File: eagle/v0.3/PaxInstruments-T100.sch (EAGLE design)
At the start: 32 parts, among them U1 Attiny85

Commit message: Added a bunch of BoM data.
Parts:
- removed L1: (no value), SeeesStudio-OPL:L-0603
- removed LOGO1: SPARKFUN-AESTHETICS_OSHW-LOGOS, PaxInstrument-T400:SPARKFUN-AESTHETICS_OSHW-LOGOS
- added R12: 0R, rcl:R-EU_R0603
- C1, C4, C5, C6, C7: MF (none) -> Yageo; MPN (none) -> CC0603JRX7R9BB104; OC_DIGIKEY (none) -> 311-1779-2-ND; POPULATE (none) -> generic; TOLERANCE (none) -> 5%
- C2, C3: POPULATE (none) -> generic
- C8: MF (none) -> Murata Electronics North America; MPN (none) -> GRM155R60J105KE19D; OC_DIGIKEY (none) -> 490-1320-2-ND; POPULATE (none) -> generic; TOLERANCE (none) -> 10%
- D1, D2: MF (none) -> Diodes Incorporated; MPN (none) -> BZT52C3V6S-7-F; OC_DIGIKEY (none) -> BZT52C3V6S-FDITR-ND; POPULATE (none) -> generic
- JP1: MF (none) -> Molex; MPN (none) -> 0480370001; OC_DIGIKEY (none) -> WM17117-ND; POPULATE (none) -> generic
- JP2: MF (none) -> FCI; MPN (none) -> 95278-101A06LF; OC_DIGIKEY (none) -> 609-3487-2-ND; POPULATE (none) -> DNP
- JP3, U$1: POPULATE (none) -> DNP
- LED1: value (none) -> Green; MF (none) -> Lite-On Inc.; MPN (none) -> LTST-C191KGKT; OC_DIGIKEY (none) -> 160-1446-2-ND; POPULATE (none) -> generic
- R1, R2: MF (none) -> Yageo; MPN (none) -> RC0603JR-0727RL; OC_DIGIKEY (none) -> 311-27GRTR-ND; POPULATE (none) -> generic; TOLERANCE (none) -> 5%
- R10: OC_DIGIKEY (none) -> 311-499DTR-ND; TOLERANCE (none) -> 0.5%
- R11: MF (none) -> Yageo; MPN (none) -> RC0603JR-070RL; OC_DIGIKEY (none) -> 311-0.0GRTR-ND; POPULATE (none) -> generic; TOLERANCE (none) -> Jumper
- R3, R4: MF (none) -> Yageo; MPN (none) -> RC0603FR-071ML; OC_DIGIKEY (none) -> 311-1.00MHRTR-ND; POPULATE (none) -> generic; TOLERANCE (none) -> 1%
- R5, R6: OC_DIGIKEY (none) -> 311-499DTR-ND; POPULATE (none) -> generic; TOLERANCE (none) -> 0.5%
- R7, R8: MF (none) -> Yageo; MPN (none) -> RC0603JR-074K7L; OC_DIGIKEY (none) -> 311-4.7KGRTR-ND; POPULATE (none) -> generic; TOLERANCE (none) -> 5%
- R9: MF (none) -> Yageo; MPN (none) -> RC0603JR-071K2L; OC_DIGIKEY (none) -> 311-1.2KGRTR-ND; POPULATE (none) -> generic; TOLERANCE (none) -> 5%
- U$3: value MCP3421 -> MCP3421A0; MF (none) -> Microchip Technology; MPN (none) -> MCP3421A0T-E/CH; OC_DIGIKEY (none) -> MCP3421A0T-E/CHTR-ND; POPULATE (none) -> MPN
- U$4: MF (none) -> Microchip Technology; MPN (none) -> MCP9800A0T-M/OT; OC_DIGIKEY (none) -> MCP9800A0T-M/OTTR-ND; POPULATE (none) -> MPN
- U$5: MF (none) -> Pax Instruments; POPULATE (none) -> MPN
- U1: MF (none) -> Atmel; MPN (none) -> ATTINY85-20SUR; OC_DIGIKEY (none) -> ATTINY85-20SURTR-ND; POPULATE (none) -> MPN
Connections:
- net A_5V: now also R12.1; no longer L1.2
- net USB_5V: now also R12.2; no longer L1.1

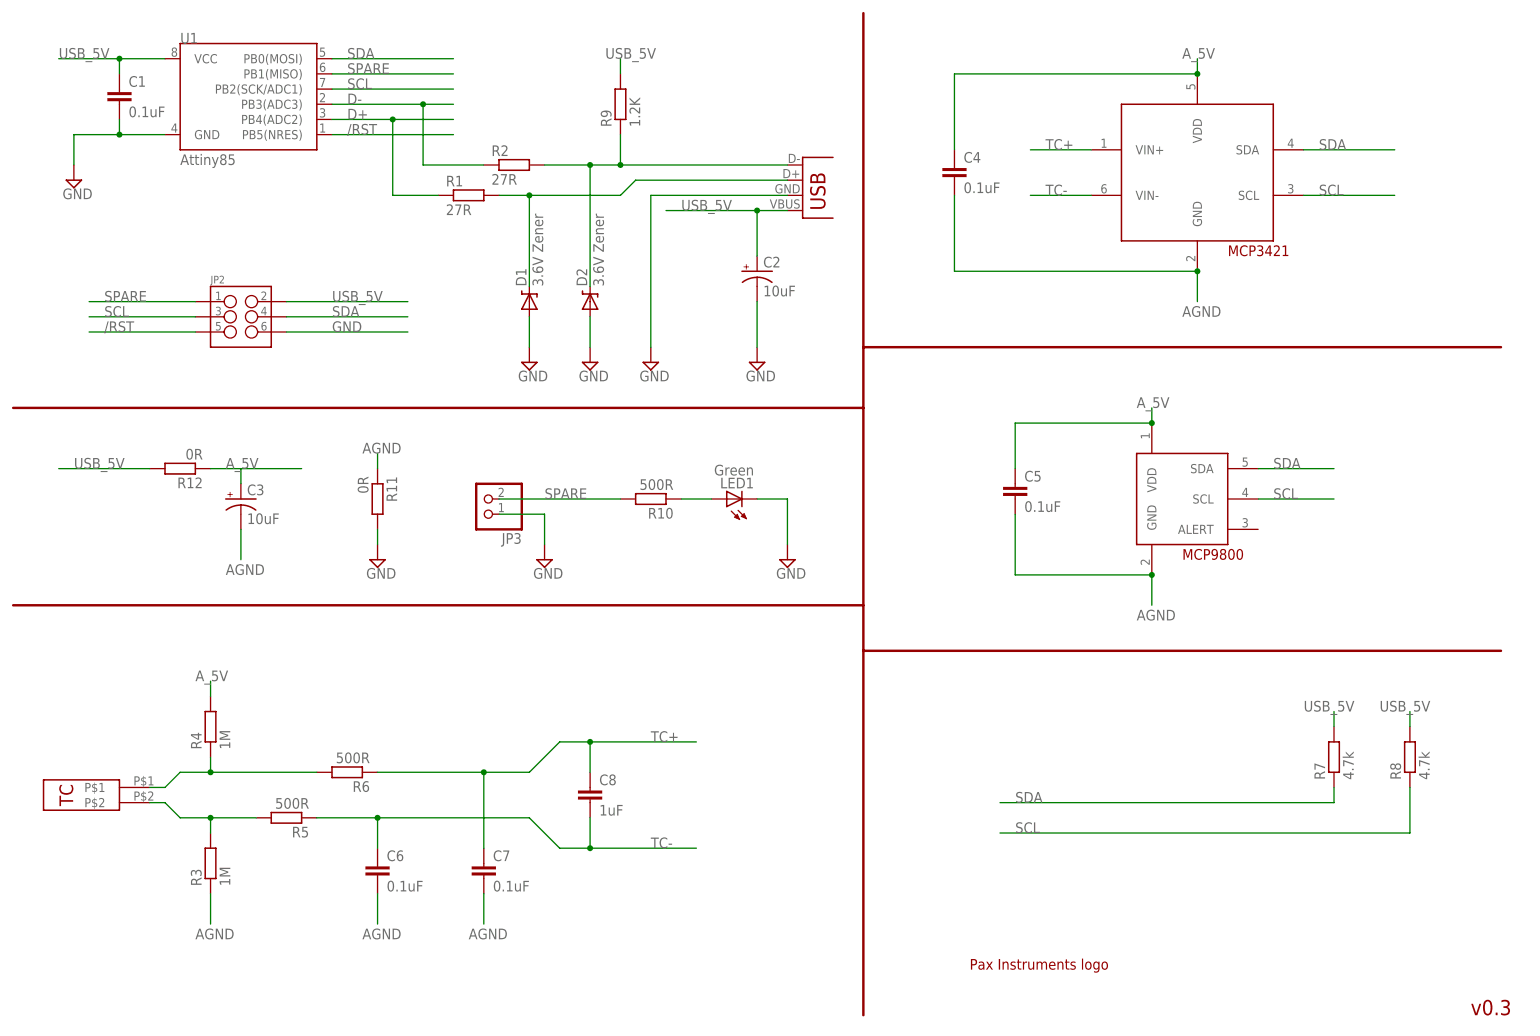
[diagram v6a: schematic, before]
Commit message: Updated thermocoupel connector. Moved MCP9800 to between the thermocouple connectors. BoM should be finished.
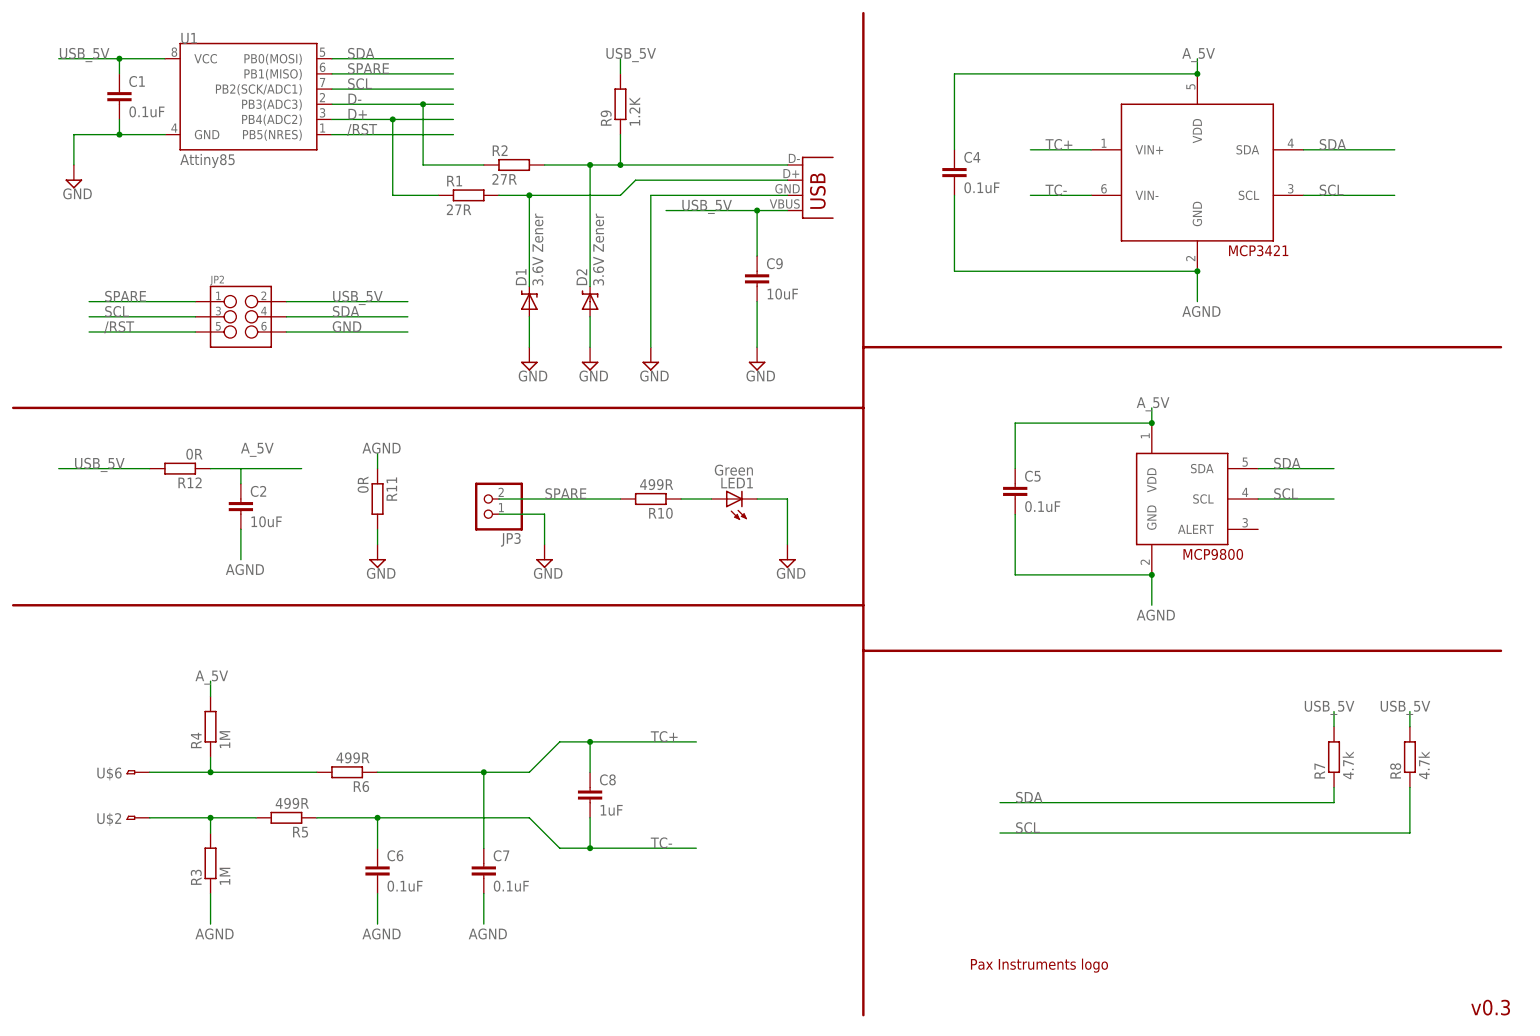
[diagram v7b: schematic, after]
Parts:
- removed C3: 10uF, SparkFun-Capacitors:10UF-TANT
- removed U$5: TC-MINI-INSIDE, PaxInstruments-Connectors:TC-MINI-INSIDE
- added C9: 10uF, SparkFun-Passives:CAP1206
- added U$2, U$6: TC-MINI-SINGLE, PaxInstruments-Connectors:TC-MINI-SINGLE
- C2: device SparkFun-Capacitors:10UF-TANT -> SparkFun-Passives:CAP1206; MF (none) -> Yageo; MPN (none) -> CC1206KKX5R7BB106; OC_DIGIKEY (none) -> 311-1465-2-ND; TOLERANCE (none) -> 10%
- R10: value 500R -> 499R; MF (none) -> Yageo; MPN (none) -> RT0603DRD07499RL; POPULATE (none) -> generic
- R5, R6: value 500R -> 499R; MF (none) -> Yageo; MPN (none) -> RT0603DRD07499RL
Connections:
- net AGND: now also C2.2; no longer C3.-
- net A_5V: now also C2.1; no longer C3.+
- net GND: now also C9.2; no longer C2.-
- net N$3: now also U$2.1; no longer U$5.P$2
- net N$4: now also U$6.1; no longer U$5.P$1
- net USB_5V: now also C9.1; no longer C2.+

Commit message: Updated thermocouple connector with th emost recent version.
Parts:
- U$2, U$6: MPN (none) -> 1024
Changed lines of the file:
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@@
 <grid distance="0.1" unitdist="inch" unit="inch" style="lines" multiple="1" display="no" altdistance="0.01" altunitdist="inch" altunit="inch"/>
 <layers>
-<layer number="1" name="Top" color="4" fill="1" visible="yes" active="no"/>
-<layer number="16" name="Bottom" color="1" fill="1" visible="yes" active="no"/>
-<layer number="17" name="Pads" color="2" fill="1" visible="yes" active="no"/>
-<layer number="18" name="Vias" color="2" fill="1" visible="yes" active="no"/>
-<layer number="19" name="Unrouted" color="6" fill="1" visible="yes" active="no"/>
-<layer number="20" name="Dimension" color="15" fill="1" visible="yes" active="no"/>
-<layer number="21" name="tPlace" color="7" fill="1" visible="yes" active="no"/>
-<layer number="22" name="bPlace" color="7" fill="1" visible="yes" active="no"/>
-<layer number="23" name="tOrigins" color="15" fill="1" visible="yes" active="no"/>
-<layer number="24" name="bOrigins" color="15" fill="1" visible="yes" active="no"/>
-<layer number="25" name="tNames" color="7" fill="1" visible="yes" active="no"/>
-<layer number="26" name="bNames" color="7" fill="1" visible="yes" active="no"/>
-<layer number="27" name="tValues" color="7" fill="1" visible="yes" active="no"/>
-<layer number="28" name="bValues" color="7" fill="1" visible="yes" active="no"/>
+<layer number="1" name="Top" color="4" fill="1" visible="no" active="no"/>
+<layer number="16" name="Bottom" color="1" fill="1" visible="no" active="no"/>
+<layer number="17" name="Pads" color="2" fill="1" visible="no" active="no"/>
+<layer number="18" name="Vias" color="2" fill="1" visible="no" active="no"/>
+<layer number="19" name="Unrouted" color="6" fill="1" visible="no" active="no"/>
+<layer number="20" name="Dimension" color="15" fill="1" visible="no" active="no"/>
+<layer number="21" name="tPlace" color="7" fill="1" visible="no" active="no"/>
+<layer number="22" name="bPlace" color="7" fill="1" visible="no" active="no"/>
+<layer number="23" name="tOrigins" color="15" fill="1" visible="no" active="no"/>
+<layer number="24" name="bOrigins" color="15" fill="1" visible="no" active="no"/>
+<layer number="25" name="tNames" color="7" fill="1" visible="no" active="no"/>
+<layer number="26" name="bNames" color="7" fill="1" visible="no" active="no"/>
+<layer number="27" name="tValues" color="7" fill="1" visible="no" active="no"/>
+<layer number="28" name="bValues" color="7" fill="1" visible="no" active="no"/>
 <layer number="29" name="tStop" color="7" fill="3" visible="no" active="no"/>
 <layer number="30" name="bStop" color="7" fill="6" visible="no" active="no"/>
@@
 <layer number="35" name="tGlue" color="7" fill="4" visible="no" active="no"/>
 <layer number="36" name="bGlue" color="7" fill="5" visible="no" active="no"/>
-<layer number="37" name="tTest" color="7" fill="1" visible="yes" active="no"/>
-<layer number="38" name="bTest" color="7" fill="1" visible="yes" active="no"/>
+<layer number="37" name="tTest" color="7" fill="1" visible="no" active="no"/>
+<layer number="38" name="bTest" color="7" fill="1" visible="no" active="no"/>
 <layer number="39" name="tKeepout" color="4" fill="11" visible="no" active="no"/>
 <layer number="40" name="bKeepout" color="1" fill="11" visible="no" active="no"/>
@@
 <layer number="44" name="Drills" color="7" fill="1" visible="no" active="no"/>
 <layer number="45" name="Holes" color="7" fill="1" visible="no" active="no"/>
-<layer number="46" name="Milling" color="3" fill="1" visible="yes" active="no"/>
-<layer number="47" name="Measures" color="7" fill="1" visible="yes" active="no"/>
-<layer number="48" name="Document" color="7" fill="1" visible="yes" active="no"/>
-<layer number="49" name="Reference" color="7" fill="1" visible="yes" active="no"/>
-<layer number="50" name="dxf" color="7" fill="1" visible="yes" active="no"/>
-<layer number="51" name="tDocu" color="7" fill="1" visible="yes" active="no"/>
-<layer number="52" name="bDocu" color="7" fill="1" visible="yes" active="no"/>
-<layer number="53" name="tGND_GNDA" color="7" fill="9" visible="yes" active="no"/>
-<layer number="54" name="bGND_GNDA" color="1" fill="9" visible="yes" active="no"/>
-<layer number="56" name="wert" color="7" fill="1" visible="yes" active="no"/>
+<layer number="46" name="Milling" color="3" fill="1" visible="no" active="no"/>
+<layer number="47" name="Measures" color="7" fill="1" visible="no" active="no"/>
+<layer number="48" name="Document" color="7" fill="1" visible="no" active="no"/>
+<layer number="49" name="Reference" color="7" fill="1" visible="no" active="no"/>
+<layer number="50" name="dxf" color="7" fill="1" visible="no" active="no"/>
+<layer number="51" name="tDocu" color="7" fill="1" visible="no" active="no"/>
+<layer number="52" name="bDocu" color="7" fill="1" visible="no" active="no"/>
+<layer number="53" name="tGND_GNDA" color="7" fill="9" visible="no" active="no"/>
+<layer number="54" name="bGND_GNDA" color="1" fill="9" visible="no" active="no"/>
+<layer number="56" name="wert" color="7" fill="1" visible="no" active="no"/>
+<layer number="57" name="tCAD" color="7" fill="1" visible="no" active="no"/>
+<layer number="59" name="tCarbon" color="7" fill="1" visible="no" active="no"/>
+<layer number="60" name="bCarbon" color="7" fill="1" visible="no" active="no"/>
 <layer number="90" name="Modules" color="5" fill="1" visible="yes" active="yes"/>
 <layer number="91" name="Nets" color="2" fill="1" visible="yes" active="yes"/>
@@
 <layer number="127" name="_tValues" color="7" fill="1" visible="yes" active="yes"/>
 <layer number="128" name="_bValues" color="7" fill="1" visible="yes" active="yes"/>
+<layer number="129" name="Mask" color="7" fill="1" visible="yes" active="yes"/>
 <layer number="131" name="tAdjust" color="7" fill="1" visible="yes" active="yes"/>
 <layer number="132" name="bAdjust" color="7" fill="1" visible="yes" active="yes"/>
 <layer number="144" name="Drill_legend" color="7" fill="1" visible="no" active="yes"/>
+<layer number="150" name="Notes" color="7" fill="1" visible="yes" active="yes"/>
 <layer number="151" name="HeatSink" color="7" fill="1" visible="no" active="yes"/>
 <layer number="152" name="_bDocu" color="7" fill="1" visible="yes" active="yes"/>
+<layer number="153" name="FabDoc1" color="7" fill="1" visible="yes" active="yes"/>
+<layer number="154" name="FabDoc2" color="7" fill="1" visible="yes" active="yes"/>
+<layer number="155" name="FabDoc3" color="7" fill="1" visible="yes" active="yes"/>
 <layer number="199" name="Contour" color="7" fill="1" visible="yes" active="yes"/>
 <layer number="200" name="200bmp" color="1" fill="10" visible="no" active="yes"/>
@@
 <layer number="223" name="223bmp" color="24" fill="1" visible="no" active="no"/>
 <layer number="224" name="224bmp" color="25" fill="1" visible="no" active="no"/>
+<layer number="225" name="225bmp" color="7" fill="1" visible="yes" active="yes"/>
+<layer number="226" name="226bmp" color="7" fill="1" visible="yes" active="yes"/>
+<layer number="227" name="227bmp" color="7" fill="1" visible="yes" active="yes"/>
+<layer number="228" name="228bmp" color="7" fill="1" visible="yes" active="yes"/>
+<layer number="229" name="229bmp" color="7" fill="1" visible="yes" active="yes"/>
+<layer number="230" name="230bmp" color="7" fill="1" visible="yes" active="yes"/>
 <layer number="231" name="Eagle3D_PG1" color="7" fill="1" visible="yes" active="yes"/>
 <layer number="232" name="Eagle3D_PG2" color="7" fill="1" visible="yes" active="yes"/>
@@
 <layer number="251" name="SMDround" color="12" fill="11" visible="no" active="no"/>
 <layer number="254" name="cooling" color="7" fill="1" visible="no" active="yes"/>
+<layer number="255" name="routoute" color="7" fill="1" visible="yes" active="yes"/>
 </layers>
 <schematic xreflabel="%F%N/%S.%C%R" xrefpart="/%S.%C%R">
@@
 <part name="U$2" library="PaxInstruments-Connectors" deviceset="TC-MINI-SINGLE" device="">
 <attribute name="MF" value="Pax Instruments"/>
+<attribute name="MPN" value="1024"/>
 <attribute name="POPULATE" value="MPN"/>
 </part>
 <part name="U$6" library="PaxInstruments-Connectors" deviceset="TC-MINI-SINGLE" device="">
 <attribute name="MF" value="Pax Instruments"/>
-<attribute name="POPULATE" value="MPN"/>
-</part>
+<attribute name="MPN" value="1024"/>
+<attribute name="POPULATE" value="MPN"/>
+</part>
